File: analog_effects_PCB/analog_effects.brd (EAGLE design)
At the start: 100 x 80 mm, 45 parts, among them J1 575-4, J2 575-4, J3 SAMTEC-SSQ-120-01-X-DJ, U1 TL082, U2 AD5241BRZ1M, U3 AD5241BRZ10, U4 AD5241BRZ100, U5 TS5A3359DCUT, U7 AD5258BRMZ1-R7

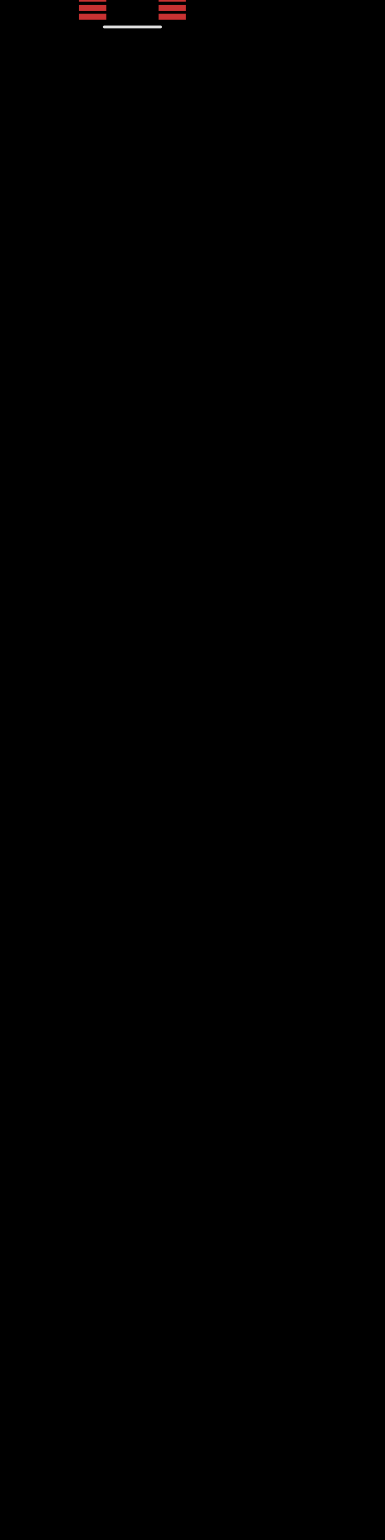
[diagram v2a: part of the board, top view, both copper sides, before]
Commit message: Added Mux logic to schematic. need to connect to Effects and decide if we have effect c or use as pass through
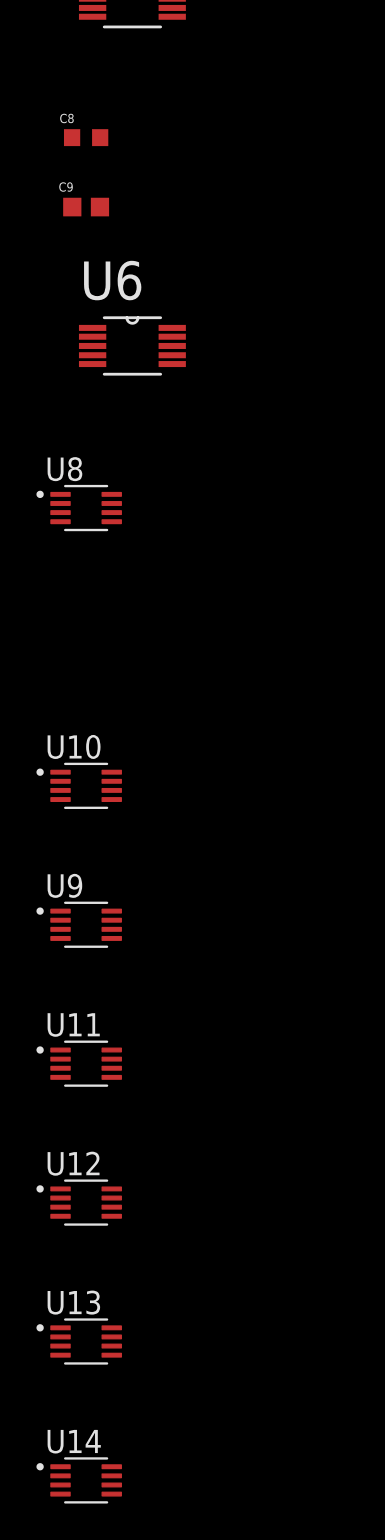
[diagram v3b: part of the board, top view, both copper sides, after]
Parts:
- added C8: GCM188R91E104KA37J, GCM188R91E104KA37J:CAPC1608X90N
- added C9: GRM188R61A226ME15D, GRM188R61A226ME15D:CAPC1608X100N
- added U10, U11, U12, U13, U14, U8, U9: TS5A3359DCUT, TS5A3359DCUT:SOP50P310X90-8N
- added U6: AD5258BRMZ1-R7, AD5258BRMZ1-R7:SOP50P490X110-10N
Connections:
- new net AUDIO_IN: U12.1, U13.1, U14.1
- new net A_OUT: U10.1, U11.1, U9.1
- new net B_OUT: U10.2, U11.2, U9.2
- new net C_OUT: U10.3, U11.3, U9.3
- new net MUX1_OUT: U10.7, U12.2, U13.2, U14.2
- new net MUX1_S1: U10.6
- new net MUX1_S2: U10.5
- new net MUX2_OUT: U12.3, U13.3, U14.3, U9.7
- new net MUX2_S1: U9.6
- new net MUX2_S2: U9.5
- new net MUX3_OUT: U11.7
- new net MUX3_S1: U11.6
- new net MUX3_S2: U11.5
- new net MUX4_OUT: U12.7
- new net MUX4_S1: U12.6
- new net MUX4_S2: U12.5
- new net MUX5_OUT: U13.7
- new net MUX5_S1: U13.6
- new net MUX5_S2: U13.5
- new net MUX6_OUT: U14.7
- new net MUX6_S1: U14.6
- new net MUX6_S2: U14.5
- new net N$29: C9.2, U7.1
- new net N$30: C8.2, U6.1
- new net N$31: U6.9
- new net N$38: U10.8
- new net N$39: U11.8
- new net N$40: U9.8
- new net N$41: U13.8
- new net N$42: U12.8
- new net N$56: U14.8
- net GND: now also C9.1, U10.4, U11.4, U12.4, U13.4, U14.4, U6.10, U6.7, U7.10, U7.7, U8.4, U9.4
- net N$18: now also C8.1
- net N$28: now also U7.9
- net VCC: now also U8.8
- net VDD: now also U6.8

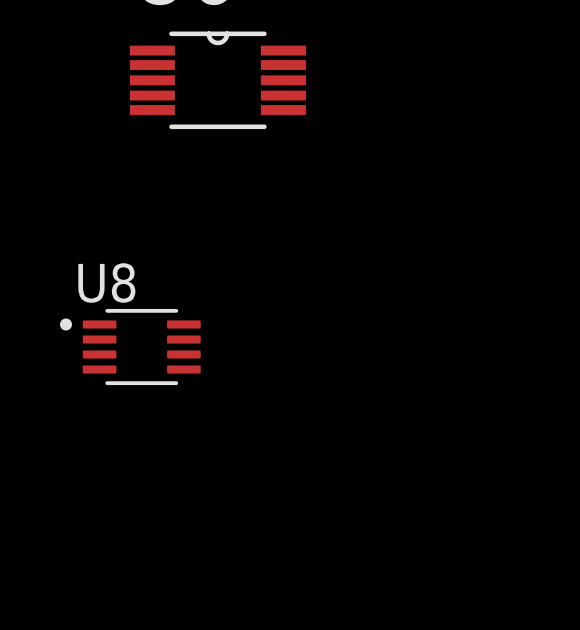
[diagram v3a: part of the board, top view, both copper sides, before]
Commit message: Fixed Fuzz pot but need to change volume pot to 500k
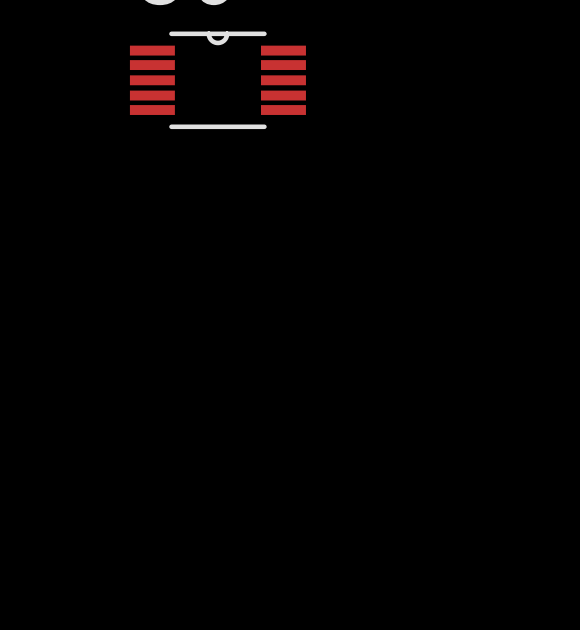
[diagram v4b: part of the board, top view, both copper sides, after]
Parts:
- removed U8: TS5A3359DCUT, TS5A3359DCUT:SOP50P310X90-8N
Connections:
- removed net FUZZ_IN: C6.1
- new net 5V: J3.1, U7.6, U7.8
- new net FUZZ_P1_SCL: U7.5
- new net FUZZ_P1_SDA: U7.4
- new net FUZZ_P2_SCL: U6.5
- new net FUZZ_P2_SDA: U6.4
- net GND: no longer U8.4
- net MUX4_OUT: now also C6.1
- net VCC: no longer U8.8
- net VDD: no longer U7.8

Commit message: Schematic almost finalized missing aux in and out and possibly push buttons, starting layout
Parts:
- removed J1, J2: 575-4, 575-4:KEYSTONE_575-4
- removed R10: 100kΩ, CRCW0603100KDHEAP:RESC1508X50N
- removed U3: AD5241BRZ10, AD5241BRZ10:SOIC127P600X175-14N
- removed U5: TS5A3359DCUT, TS5A3359DCUT:SOP50P310X90-8N
- removed U6: AD5258BRMZ1-R7, AD5258BRMZ1-R7:SOP50P490X110-10N
- added C10, C11, C12, C13, C14, C15, C16, C17, C18, C19, C20, C21: GCM188R91E104KA37J, GCM188R91E104KA37J:CAPC1608X90N
- added TP10, TP11, TP12, TP13, TP14, TP15, TP16, TP17, TP18, TP19, TP20, TP7, TP8, TP9: 5015, 5015:KEYSTONE_5015
- added U8: AD5241BRZ1M, AD5241BRZ1M:SOIC127P600X175-14N
- R11, R12, R13, R14, R15, R7, R8, R9: value 100kΩ -> 10kΩ; device CRCW0603100KDHEAP:RESC1508X50N -> MCT06030D1002BP100:RESC1508X55N
- moved U14 313.3 mm to (31.8, 8.89)
- moved U13 311.3 mm to (40.6, 8.89)
- moved U12 309.6 mm to (49.5, 8.89)
- moved U11 308.4 mm to (58.4, 8.89)
- moved U9 307.6 mm to (67.3, 8.89)
- moved U10 307.3 mm to (76.2, 8.89)
- moved R11 247.7 mm to (-134.6, -284.5)
- moved R12 247.7 mm to (-134.6, -288.3)
- moved R13 217.5 mm to (-134.6, -292.1)
- moved R14 217.5 mm to (-134.6, -295.9)
- moved R15 217.5 mm to (-134.6, -299.7)
- moved R7 187.1 mm to (-134.6, -273.1)
- moved R8 187.1 mm to (-134.6, -276.9)
- moved R9 187.1 mm to (-134.6, -280.7)
- moved J3 178.4 mm to (90.2, 43.2), turned to 270 degrees
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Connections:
- removed net FUZZ_P1_SCL: U7.5
- removed net FUZZ_P1_SDA: U7.4
- removed net FUZZ_P2_SCL: U6.5
- removed net FUZZ_P2_SDA: U6.4
- removed net N$16: C5.2, U3.3
- removed net N$24: R7.1, U3.7
- removed net N$25: R7.2, R8.2, R9.2, U3.4
- removed net N$26: R9.1, U3.5
- removed net N$27: R8.1, U3.6
- removed net N$31: U6.9
- removed net N$38: U10.8
- removed net N$39: U11.8
- removed net N$40: U9.8
- removed net N$41: U13.8
- removed net N$42: U12.8
- removed net N$56: U14.8
- removed net VCC: U5.8
- removed net VDD: U6.8
- new net POT_SCL: J3.5, R11.2, R12.2, R14.2, R7.2
- new net POT_SDA: J3.3, R13.1, R15.1, R8.1, R9.1
- net 5V: now also C10.2, C11.2, C12.2, C13.2, C14.2, C15.2, C16.2, C17.2, C18.2, C19.2, C20.2, C21.2, J3.2, TP19.1, TP20.1, U10.8, U11.8, U12.8, U13.8, U14.8, U2.4, U2.5, U4.4, U4.5, U4.9, U7.2, U7.3, U8.4, U8.5, U8.8, U9.8; no longer J3.1
- net A_OUT: now also TP12.1, U8.3
- net B_OUT: now also U4.2
- net GND: now also C10.1, C11.1, C12.1, C13.1, C14.1, C15.1, C16.1, C17.1, C18.1, C19.1, C20.1, C21.1, J3.39, U8.10, U8.11, U8.9; no longer J2.1, U3.10, U3.11, U3.8, U3.9, U4.2, U4.9, U5.4, U6.10, U6.7
- net MUX1_OUT: now also TP16.1
- net MUX1_S1: now also J3.7
- net MUX1_S2: now also J3.29
- net MUX2_OUT: now also TP17.1
- net MUX2_S1: now also J3.31
- net MUX2_S2: now also J3.26
- net MUX3_OUT: now also TP18.1
- net MUX3_S1: now also J3.24
- net MUX3_S2: now also J3.21
- net MUX4_OUT: now also TP13.1
- net MUX4_S1: now also J3.19
- net MUX4_S2: now also J3.23
- net MUX5_OUT: now also R1.1, TP14.1
- net MUX5_S1: now also J3.32
- net MUX5_S2: now also J3.33
- net MUX6_OUT: now also TP15.1
- net MUX6_S1: now also J3.8
- net MUX6_S2: now also J3.10
- net N$10: now also TP8.1
- net N$11: now also TP9.1
- net N$12: now also R8.2, U2.7; no longer R10.1, U2.5
- net N$14: now also R12.1, U8.6; no longer R11.2, U2.7
- net N$15: now also R9.2, U4.7; no longer R10.2, R11.1, R12.2, U2.4
- net N$17: now also R7.1; no longer R12.1
- net N$19: now also R13.2, U8.7; no longer R13.1, U4.7
- net N$20: now also R14.1, U7.5; no longer R13.2, R14.2, R15.2, U4.4
- net N$21: now also R11.1; no longer R15.1
- net N$22: now also C5.2; no longer U3.2
- net N$23: now also R15.2, U7.4; no longer R14.1, U4.5
- net N$29: now also TP11.1
- net N$30: now also TP10.1, U8.1; no longer U6.1
- net N$8: now also R18.2; no longer J1.1, R1.1
- net N$9: now also TP7.1

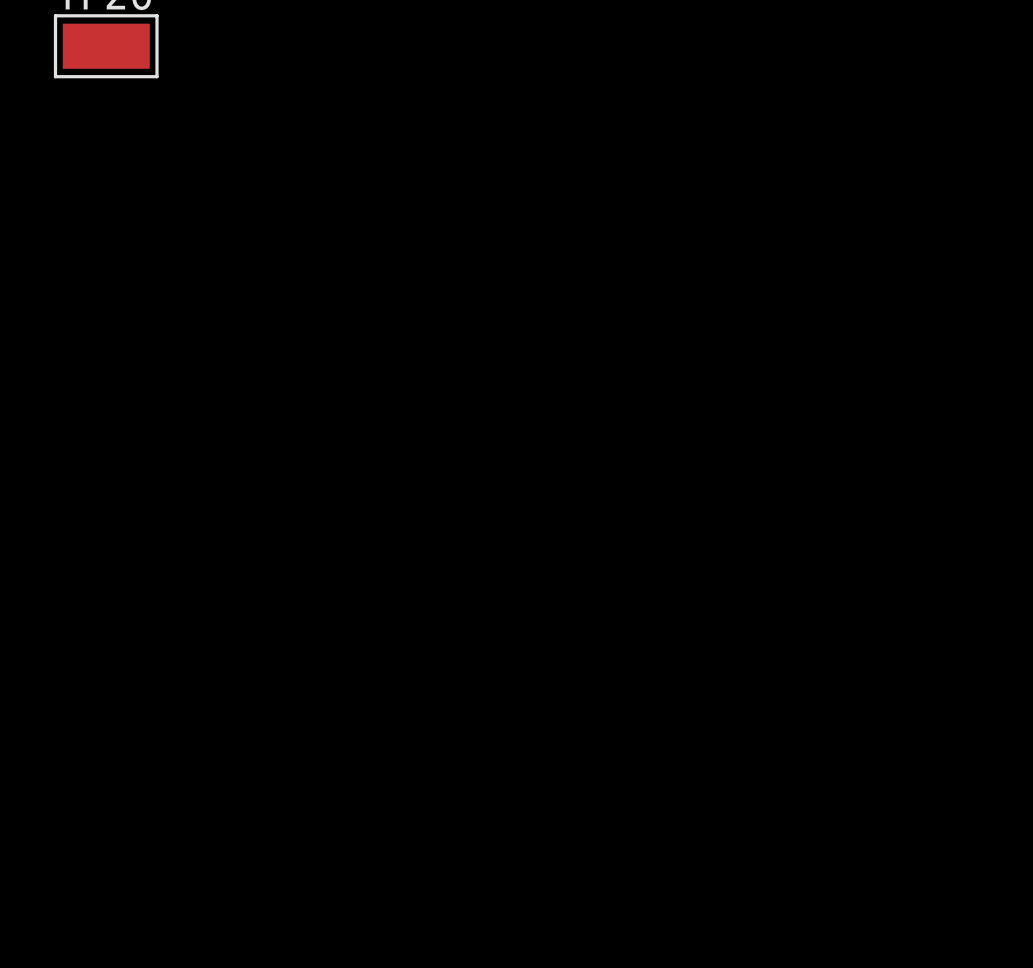
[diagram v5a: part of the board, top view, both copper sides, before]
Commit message: Finalized schematic with connectos, next step layout
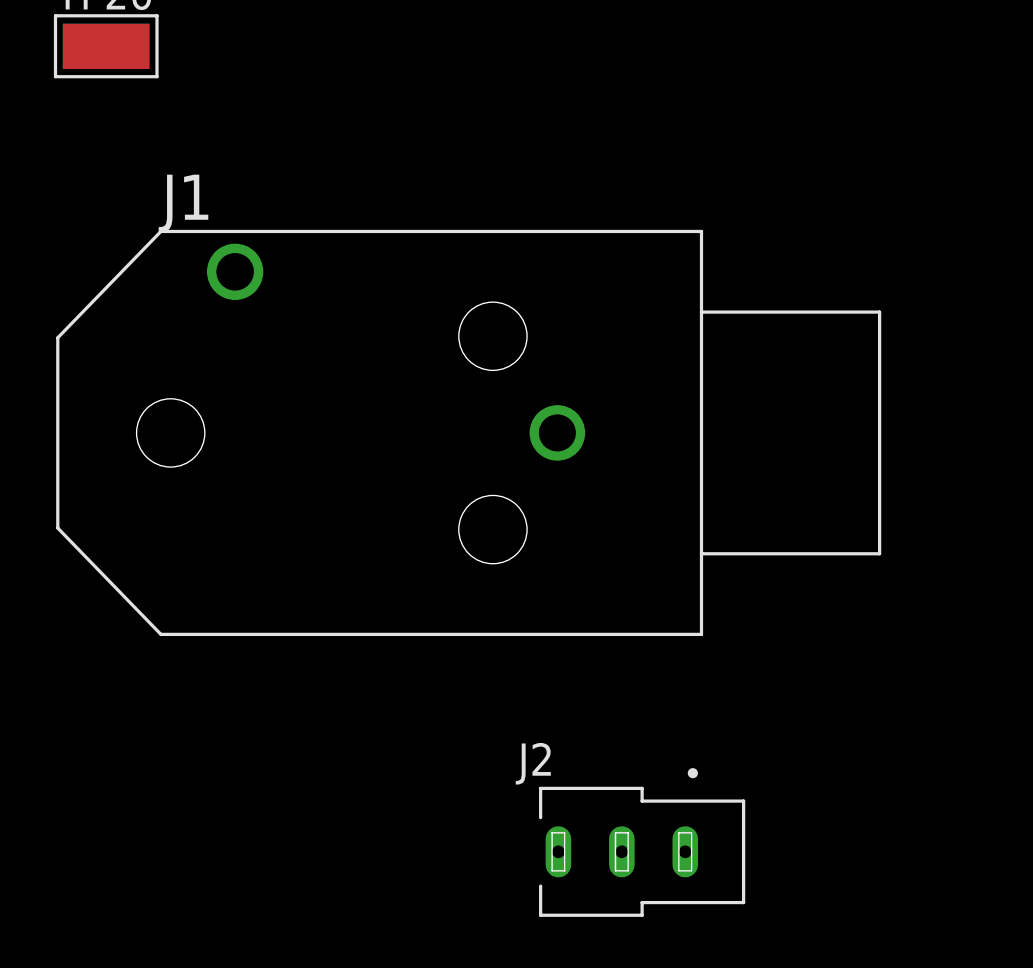
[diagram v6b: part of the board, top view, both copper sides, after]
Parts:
- added J1: RN111PC, RN111PC:SWITCHCRAFT_RN111PC
- added J2: SP-3533-02, SP-3533-02:CUI_SP-3533-02
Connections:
- net AUDIO_IN: now also J1.T
- net GND: now also J1.S, J2.3
- net MUX6_OUT: now also J2.1, J2.2
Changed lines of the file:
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@@
 <attribute name="VALUE" x="-136.62248125" y="-467.52335" size="1.27156875" layer="27"/>
+</element>
+<element name="J1" library="RN111PC" package="SWITCHCRAFT_RN111PC" value="RN111PC" x="-116.84" y="-480.06" smashed="yes">
+<attribute name="AVAILABILITY" value="Good" x="-116.84" y="-480.06" size="1.778" layer="27" display="off"/>
+<attribute name="DESCRIPTION" value=" 6.35mm (0.250, 1/4) - Headphone Phone Jack Mono Connector Solder " x="-116.84" y="-480.06" size="1.778" layer="27" display="off"/>
+<attribute name="MF" value="Switchcraft" x="-116.84" y="-480.06" size="1.778" layer="27" display="off"/>
+<attribute name="MP" value="RN111PC" x="-116.84" y="-480.06" size="1.778" layer="27" display="off"/>
+<attribute name="NAME" x="-132.44" y="-471.66" size="1.778" layer="25"/>
+<attribute name="PACKAGE" value="None" x="-116.84" y="-480.06" size="1.778" layer="27" display="off"/>
+<attribute name="PRICE" value="None" x="-116.84" y="-480.06" size="1.778" layer="27" display="off"/>
+<attribute name="PURCHASE-URL" value="https://pricing.snapeda.com/search/part/RN111PC/?ref=eda" x="-116.84" y="-480.06" size="1.778" layer="27" display="off"/>
+<attribute name="VALUE" x="-132.44" y="-490.26" size="1.778" layer="27"/>
+</element>
+<element name="J2" library="SP-3533-02" package="CUI_SP-3533-02" value="SP-3533-02" x="-114.3" y="-496.57" smashed="yes">
+<attribute name="AVAILABILITY" value="Warning" x="-114.3" y="-496.57" size="1.778" layer="27" display="off"/>
+<attribute name="CUI_PURCHASE_URL" value="https://www.cuidevices.com/product/interconnect/connectors/audio-connectors/audio-plugs/sp-3533-02?utm_source=snapeda.com&amp;utm_medium=referral&amp;utm_campaign=snapedaBOM" x="-114.3" y="-496.57" size="1.778" layer="27" display="off"/>
+<attribute name="DESCRIPTION" value="3.5 mm, Stereo, PCB Mount, Through Hole, Audio Plug Connector" x="-114.3" y="-496.57" size="1.778" layer="27" display="off"/>
+<attribute name="MF" value="CUI Devices" x="-114.3" y="-496.57" size="1.778" layer="27" display="off"/>
+<attribute name="MP" value="SP-3533-02" x="-114.3" y="-496.57" size="1.778" layer="27" display="off"/>
+<attribute name="NAME" x="-118.4" y="-493.57" size="1.27" layer="25"/>
+<attribute name="PACKAGE" value="None" x="-114.3" y="-496.57" size="1.778" layer="27" display="off"/>
+<attribute name="PRICE" value="None" x="-114.3" y="-496.57" size="1.778" layer="27" display="off"/>
+<attribute name="PURCHASE-URL" value="https://pricing.snapeda.com/search/part/SP-3533-02/?ref=eda" x="-114.3" y="-496.57" size="1.778" layer="27" display="off"/>
+<attribute name="VALUE" x="-118.4" y="-499.57" size="1.27" layer="27" align="top-left"/>
 </element>
 </elements>
@@
 <contactref element="C20" pad="1"/>
 <contactref element="C21" pad="1"/>
+<contactref element="J1" pad="S"/>
+<contactref element="J2" pad="3"/>
 <wire x1="-135.39" y1="-341.63" x2="-135.39" y2="-345.44" width="0" layer="19" extent="1-1"/>
 <wire x1="-135.39" y1="-337.82" x2="-135.39" y2="-341.63" width="0" layer="19" extent="1-1"/>
@@
 <wire x1="74.795" y1="8.14" x2="65.905" y2="8.14" width="0" layer="19" extent="1-1"/>
 <wire x1="91.44" y1="19.05" x2="74.795" y2="8.14" width="0" layer="19" extent="1-1"/>
+<wire x1="-116.84" y1="-480.06" x2="-135.39" y2="-345.44" width="0" layer="19" extent="1-1"/>
+<wire x1="-116.8" y1="-496.57" x2="-116.84" y2="-480.06" width="0" layer="19" extent="1-1"/>
 </signal>
 <signal name="N$4">
@@
 <contactref element="U14" pad="7"/>
 <contactref element="TP15" pad="1"/>
-<wire x1="-134.62" y1="-426.72" x2="33.155" y2="9.14" width="0" layer="19" extent="1-1"/>
+<contactref element="J2" pad="2"/>
+<contactref element="J2" pad="1"/>
+<wire x1="-111.8" y1="-496.57" x2="-114.3" y2="-496.57" width="0" layer="19" extent="1-1"/>
+<wire x1="-134.62" y1="-426.72" x2="-114.3" y2="-496.57" width="0" layer="19" extent="1-1"/>
+<wire x1="33.155" y1="9.14" x2="-134.62" y2="-426.72" width="0" layer="19" extent="1-1"/>
 </signal>
 <signal name="AUDIO_IN">
@@
 <contactref element="U13" pad="1"/>
 <contactref element="U14" pad="1"/>
+<contactref element="J1" pad="T"/>
+<wire x1="30.345" y1="9.64" x2="-129.54" y2="-473.71" width="0" layer="19" extent="1-1"/>
 <wire x1="39.235" y1="9.64" x2="30.345" y2="9.64" width="0" layer="19" extent="1-1"/>
 <wire x1="48.125" y1="9.64" x2="39.235" y2="9.64" width="0" layer="19" extent="1-1"/>

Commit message: Adding all files that were needed, Capstone is completed and it worked
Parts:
- removed BT1, BT2: BC9VPC, BC9VPC:BAT_BC9VPC
- removed J2: SP-3533-02, SP-3533-02:CUI_SP-3533-02
- added J4: SJ-3523-SMT-TR, SJ-3523-SMT-TR:CUI_SJ-3523-SMT-TR
- added R10, R20, R21, R22, R23, R24, R25, R26, R27, R28, R29, R30: MCT06030D1002BP100, MCT06030D1002BP100:RESC1508X55N
- moved J1 536.3 mm to (97.8, 11.4)
- moved C21 470.9 mm to (80.0, 73.7), turned to 90 degrees
- moved C20 465.7 mm to (76.2, 73.7), turned to 90 degrees
- moved C19 460.6 mm to (72.4, 73.7), turned to 90 degrees
- moved C18 455.5 mm to (68.6, 73.7), turned to 90 degrees
- moved C17 450.4 mm to (64.8, 73.7), turned to 90 degrees
- moved C16 445.3 mm to (61.0, 73.7), turned to 90 degrees
- moved C15 440.2 mm to (57.1, 73.7), turned to 90 degrees
- moved C14 435.1 mm to (53.3, 73.7), turned to 90 degrees
- moved C13 430.0 mm to (49.5, 73.7), turned to 90 degrees
- moved C12 425.0 mm to (45.7, 73.7), turned to 90 degrees
- moved C11 419.9 mm to (41.9, 73.7), turned to 90 degrees
- moved C10 414.9 mm to (38.1, 73.7), turned to 90 degrees
- moved U4 164.9 mm to (14.0, 30.5)
- moved U2 111.6 mm to (26.7, 27.9)
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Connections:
- removed net N$11: BT2.N, R17.2, R19.2, TP9.1
- new net 9V_N: C4.2, C7.2, R17.2, R19.2, R5.1, TP2.1, TP9.1
- net 5V: now also R10.2, R20.2, R21.2, R22.2, R23.2, R24.2, R25.2, R26.2, R27.2, R28.2, R29.2, R30.2
- net GND: now also J4.1; no longer BT1.N, C4.2, C7.2, J2.3, R5.1, TP2.1
- net MUX1_S1: now also R10.1
- net MUX1_S2: now also R20.1
- net MUX2_S1: now also R21.1
- net MUX2_S2: now also R22.1
- net MUX3_S1: now also R23.1
- net MUX3_S2: now also R24.1
- net MUX4_S1: now also R25.1
- net MUX4_S2: now also R26.1
- net MUX5_S1: now also R27.1
- net MUX5_S2: now also R28.1
- net MUX6_OUT: now also J4.2, J4.3; no longer J2.1, J2.2
- net MUX6_S1: now also R29.1
- net MUX6_S2: now also R30.1
- net N$1: no longer BT1.P
